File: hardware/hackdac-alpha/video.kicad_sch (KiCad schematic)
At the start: 86 parts, among them J1 VIDEO OUT, U1 AD768, U2 MAX4104, U3 TLE2082, U4 MAX4104

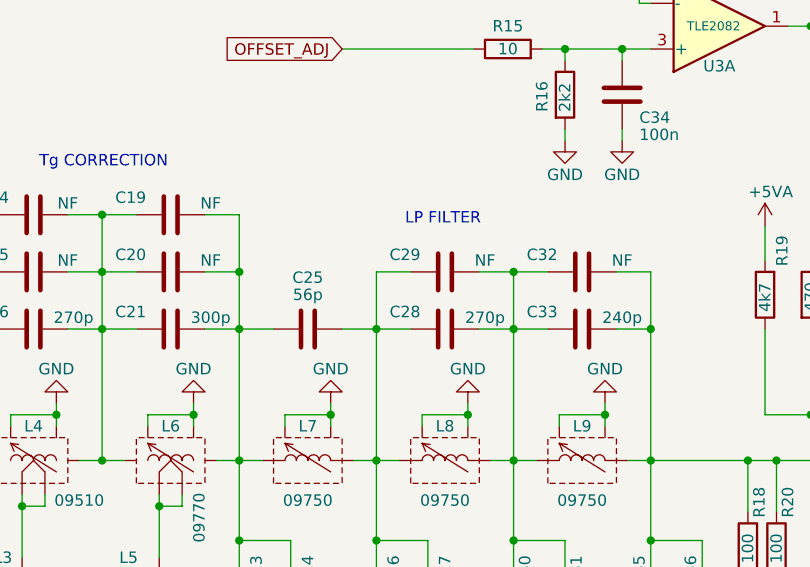
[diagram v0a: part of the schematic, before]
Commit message: Fixed a couple of incorrect component values
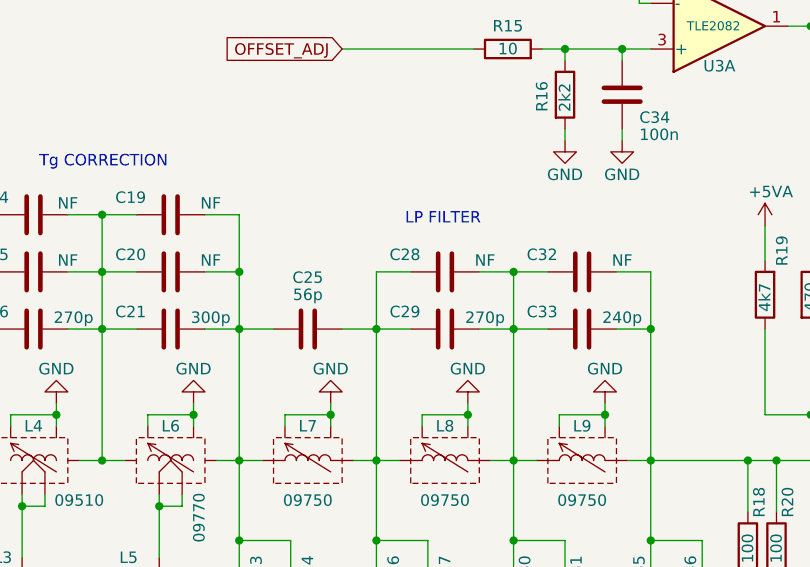
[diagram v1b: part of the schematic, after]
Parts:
- C28: value 270p -> NF
- C29: value NF -> 270p
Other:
- moved on the sheet: C28, C29
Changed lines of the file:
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@@
 	(symbol
 		(lib_id "Device:C")
-		(at 202.565 72.39 90)
+		(at 202.565 66.04 90)
 		(unit 1)
 		(exclude_from_sim no)
@@
 		(dnp no)
 		(property "Reference" "C28"
-			(at 198.12 70.485 90)
-			(effects
-				(font
-					(size 1.27 1.27)
-				)
-			)
-		)
-		(property "Value" "270p"
-			(at 207.01 71.12 90)
+			(at 198.12 64.135 90)
+			(effects
+				(font
+					(size 1.27 1.27)
+				)
+			)
+		)
+		(property "Value" "NF"
+			(at 207.01 64.77 90)
 			(effects
 				(font
@@
 		)
 		(property "Footprint" "Capacitor_SMD:C_0603_1608Metric"
-			(at 206.375 71.4248 0)
+			(at 206.375 65.0748 0)
 			(effects
 				(font
@@
 		)
 		(property "Datasheet" "~"
-			(at 202.565 72.39 0)
-			(effects
-				(font
-					(size 1.27 1.27)
-				)
-				(hide yes)
-			)
-		)
-		(property "Description" ""
-			(at 202.565 72.39 0)
+			(at 202.565 66.04 0)
+			(effects
+				(font
+					(size 1.27 1.27)
+				)
+				(hide yes)
+			)
+		)
+		(property "Description" ""
+			(at 202.565 66.04 0)
 			(effects
 				(font
@@
 	(symbol
 		(lib_id "Device:C")
-		(at 202.565 66.04 90)
+		(at 202.565 72.39 90)
 		(unit 1)
 		(exclude_from_sim no)
@@
 		(dnp no)
 		(property "Reference" "C29"
-			(at 198.12 64.135 90)
-			(effects
-				(font
-					(size 1.27 1.27)
-				)
-			)
-		)
-		(property "Value" "NF"
-			(at 207.01 64.77 90)
+			(at 198.12 70.485 90)
+			(effects
+				(font
+					(size 1.27 1.27)
+				)
+			)
+		)
+		(property "Value" "270p"
+			(at 207.01 71.12 90)
 			(effects
 				(font
@@
 		)
 		(property "Footprint" "Capacitor_SMD:C_0603_1608Metric"
-			(at 206.375 65.0748 0)
+			(at 206.375 71.4248 0)
 			(effects
 				(font
@@
 		)
 		(property "Datasheet" "~"
-			(at 202.565 66.04 0)
-			(effects
-				(font
-					(size 1.27 1.27)
-				)
-				(hide yes)
-			)
-		)
-		(property "Description" ""
-			(at 202.565 66.04 0)
-			(effects
-				(font
+			(at 202.565 72.39 0)
+			(effects
+				(font
+					(size 1.27 1.27)
+				)
+				(hide yes)
+			)
+		)
+		(property "Description" ""
+			(at 202.565 72.39 0)
+			(effects
+				(font
